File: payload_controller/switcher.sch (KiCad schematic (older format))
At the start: 60 parts, among them J1 Silicon Cell, J2 G125-MH12605M4R, Q1 DMC2053UVT, U1 SN74LVC1G14DRL, U10 MAX4736EUBT, U11 MAX4736EUBT, U12 MAX4736EUBT, U13 MAX4736EUBT, U14 MAX4736EUBT, U19 MAX4736EUBT, U2 CD4518BM96, U3 CD4028BMT, U30 LT3092EDD#TRPBF, U4 CD4028BMT, U5 MAX4736EUBT, U6 MAX4736EUBT, U7 MAX4736EUBT, U8 MAX4736EUBT, U9 MAX4736EUBT

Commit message: Continuing layout
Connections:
- net GND: now also U19.4 (NO2), U19.9 (NC1); no longer U19.2 (NO1), U19.7 (NC2)
- net PANEL_POSITIVE: now also U19.2 (NO1), U19.7 (NC2); no longer U19.4 (NO2), U19.9 (NC1)
- net at U19.10 (COM1): now also U10.2 (NO1), U10.4 (NO2), U11.2 (NO1), U11.4 (NO2), U12.2 (NO1), U12.4 (NO2), U13.2 (NO1), U13.4 (NO2), U14.2 (NO1), U14.4 (NO2), U5.2 (NO1), U5.4 (NO2), U6.2 (NO1), U6.4 (NO2), U7.2 (NO1), U7.4 (NO2), U8.2 (NO1), U8.4 (NO2), U9.2 (NO1), U9.4 (NO2); no longer J2.1 (CP)
- new net: J2.1 (CP), U19.6 (COM2)
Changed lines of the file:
@@
 Wire Wire Line
 	9650 2050 9650 2150
-Wire Wire Line
-	10850 2850 10850 1950
-Wire Wire Line
-	10850 1950 10650 1950
 Connection ~ 10850 2850
-$Comp
-L power:GND #PWR?
-U 1 1 637B130F
-P 10750 2250
-AR Path="/6313FC31/637B130F" Ref="#PWR?"  Part="1"
-AR Path="/637B130F" Ref="#PWR?"  Part="1"
-AR Path="/635FE71D/637B130F" Ref="#PWR0242"  Part="1"
-F 0 "#PWR0242" H 10750 2000 50  0001 C CNN
-F 1 "GND" H 10755 2077 50  0000 C CNN
-F 2 "" H 10750 2250 50  0001 C CNN
-F 3 "" H 10750 2250 50  0001 C CNN
-	1    10750 2250
-	-1   0    0    -1
-$EndComp
-Wire Wire Line
-	10650 2050 10750 2050
-Wire Wire Line
-	10750 2050 10750 1850
-Wire Wire Line
-	10750 1850 10650 1850
-Connection ~ 10750 2050
-Wire Wire Line
-	10750 2050 10750 2250
-Wire Wire Line
-	10650 2150 10900 2150
-Wire Wire Line
-	10900 2150 10900 1950
-Wire Wire Line
-	10900 1750 10650 1750
-Wire Wire Line
-	10900 1950 12050 1950
-Text HLabel 12050 1950 2    50   Output ~ 0
+Text HLabel 12200 1850 2    50   Output ~ 0
 PANEL_POSITIVE
-Connection ~ 10900 1950
-Wire Wire Line
-	10900 1950 10900 1750
 Wire Wire Line
 	9750 1850 9650 1850
@@
 ALERT
 Wire Wire Line
-	10650 1650 15900 1650
-Wire Wire Line
-	15900 1650 15900 5900
-Wire Wire Line
 	15900 5900 18950 5900
 Wire Wire Line
@@
 Wire Wire Line
 	8300 4350 8400 4350
+$Comp
+L power:GND #PWR?
+U 1 1 637B130F
+P 10750 2250
+AR Path="/6313FC31/637B130F" Ref="#PWR?"  Part="1"
+AR Path="/637B130F" Ref="#PWR?"  Part="1"
+AR Path="/635FE71D/637B130F" Ref="#PWR0242"  Part="1"
+F 0 "#PWR0242" H 10750 2000 50  0001 C CNN
+F 1 "GND" H 10755 2077 50  0000 C CNN
+F 2 "" H 10750 2250 50  0001 C CNN
+F 3 "" H 10750 2250 50  0001 C CNN
+	1    10750 2250
+	-1   0    0    -1
+$EndComp
+Wire Wire Line
+	10850 1650 10650 1650
+Wire Wire Line
+	10850 1650 10850 2850
+Wire Wire Line
+	10650 1950 15900 1950
+Wire Wire Line
+	15900 1950 15900 5900
+Wire Wire Line
+	10750 1750 10750 2150
+Wire Wire Line
+	10750 1750 10650 1750
+Wire Wire Line
+	10650 2150 10750 2150
+Connection ~ 10750 2150
+Wire Wire Line
+	10750 2150 10750 2250
+Wire Wire Line
+	10650 1850 11000 1850
+Wire Wire Line
+	10650 2050 11000 2050
+Wire Wire Line
+	11000 2050 11000 1850
+Connection ~ 11000 1850
+Wire Wire Line
+	11000 1850 12200 1850
 $EndSCHEMATC

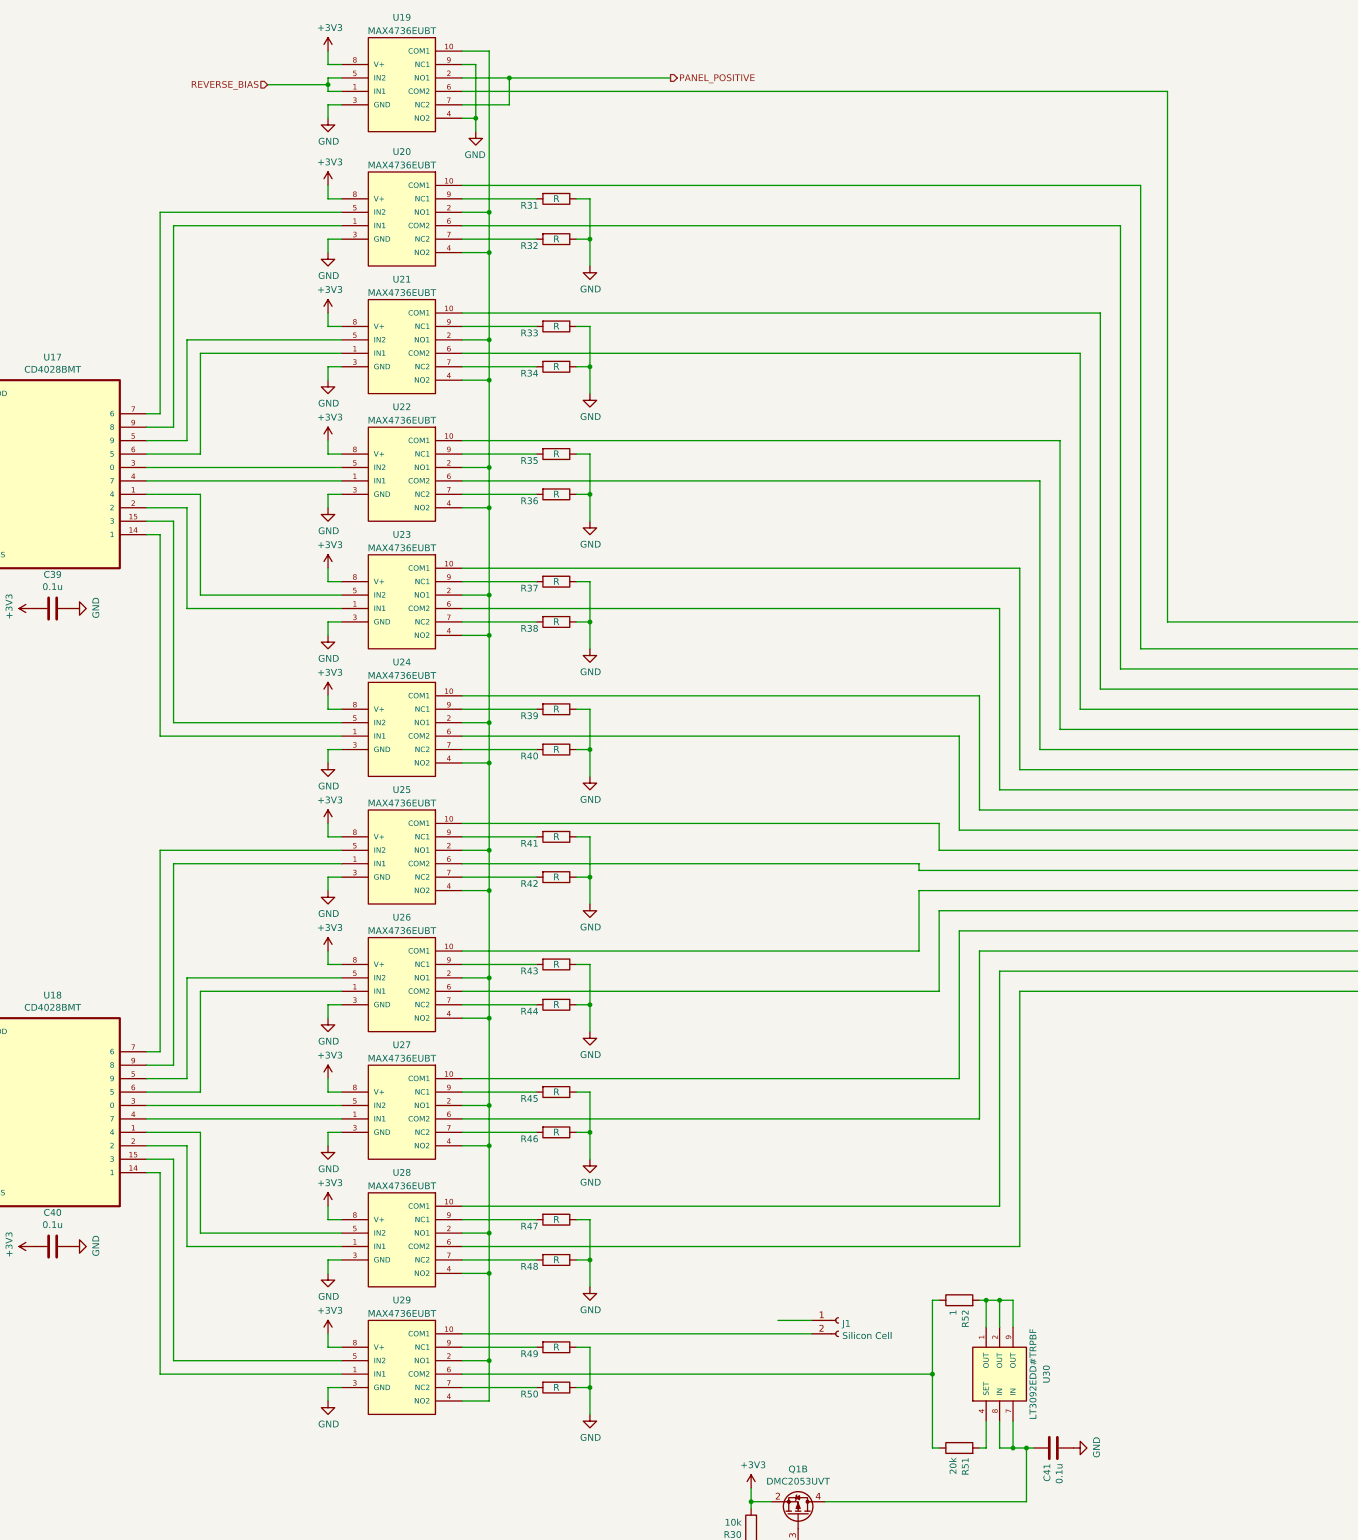
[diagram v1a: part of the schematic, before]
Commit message: Continuing payload design
- Add OR gate for reverse bias
- Add GaAs panel connectors
- Add 3D models
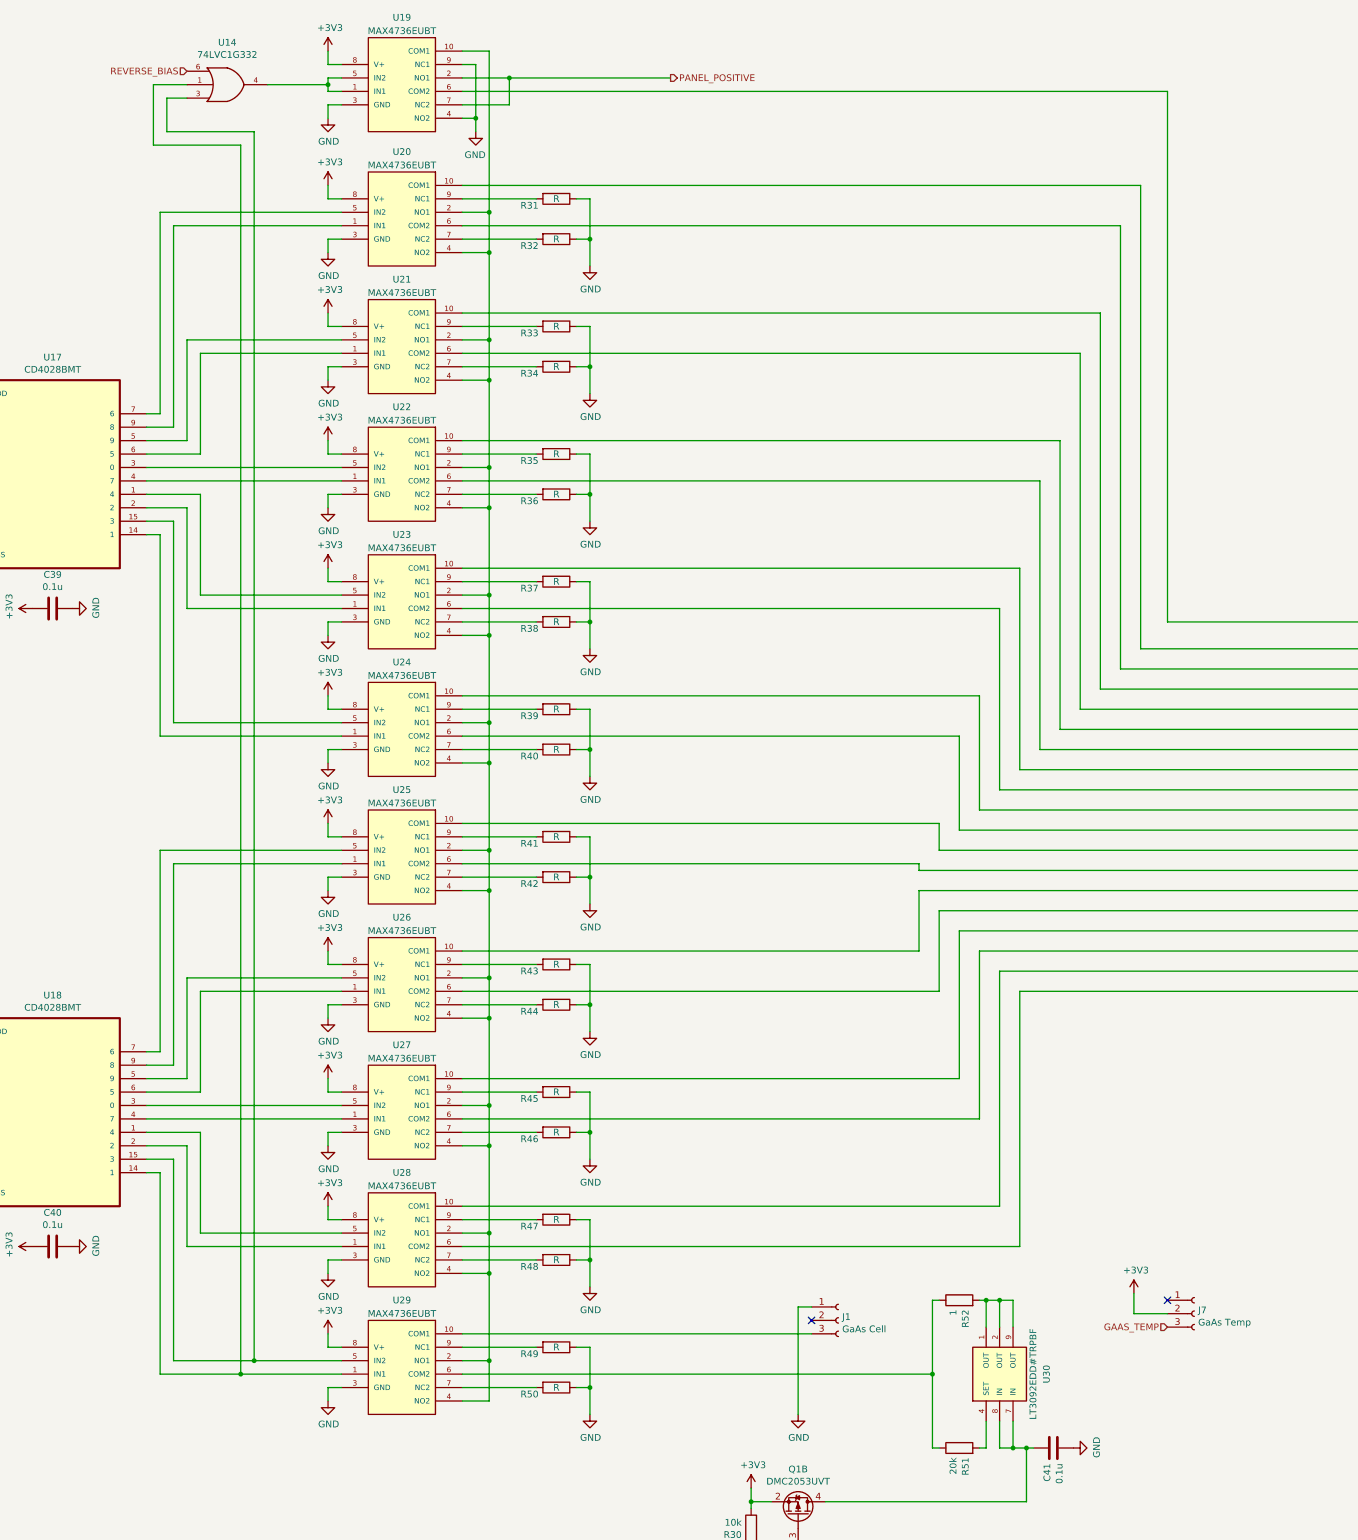
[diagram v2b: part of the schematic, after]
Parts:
- removed J1: Silicon Cell, Connector_PinHeader_2.54mm:PinHeader_1x02_P2.54mm_Vertical, symbol Connector:Conn_01x02_Female
- added J1: GaAs Cell, DF13C-3P-1:HRS_DF13C-3P-1.25V(21), symbol Connector:Conn_01x03_Female
- added J7: GaAs Temp, DF13C-3P-1:HRS_DF13C-3P-1.25V(21), symbol Connector:Conn_01x03_Female
- added U14: 74LVC1G332, ul_ADG841YKSZ-500RL7:ADG841YKSZ-500RL7, symbol ADG841YKSZ-500RL7:74LVC1G332
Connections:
- net +3V3: now also J7.2 (Pin_2), U14.5 (+3V3)
- net GND: now also J1.1 (Pin_1), U14.2 (GND)
- net REVERSE_BIAS: now also U14.6; no longer U19.1 (IN1), U19.5 (IN2)
- net at U14.10 (COM1): now also J1.3 (Pin_3)
- net at U14.1 (IN1), U4.14 (1): now also U14.1
- net at U14.5 (IN2), U4.15 (3): now also U14.3
- new net: U14.4, U19.1 (IN1), U19.5 (IN2)
- new net GAAS_TEMP: J7.3 (Pin_3)
- no-connect marks 0 -> 2
